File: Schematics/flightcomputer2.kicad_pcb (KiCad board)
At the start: 4 copper layers, 80 x 80 mm, 105 parts, among them J1 Microsemi_FlashPro-JTAG-10, J10 Pyro, J2 Pyro, J4 Drouge, J5 Conn_01x05_Pin, J6 Conn_01x05_Pin, J7 Conn_Coaxial_Small, J8 Micro_SD_Card, J9 USB_C_Receptacle_USB2.0_16P, Q1 IRLML2502TRPBF, Q2 IRLML2502TRPBF, Q3 BC817, Q4 IRLML2502TRPBF, Q6 Q_PMOS_GSD, SW1 SAMZO G4R0015010, SW2 SAMZO G4R0015010, U1 STM32F405RGT6, U2 SN65HVD230, U3 PowerIn, U4 LDL1117-3.3, U5 RFM95W-915S2, U6 Bosch BMP388, U7 LSM6DS3TR-C, U8 W25Q128JVP, U9 H3LIS331DL, Y1 8mhz

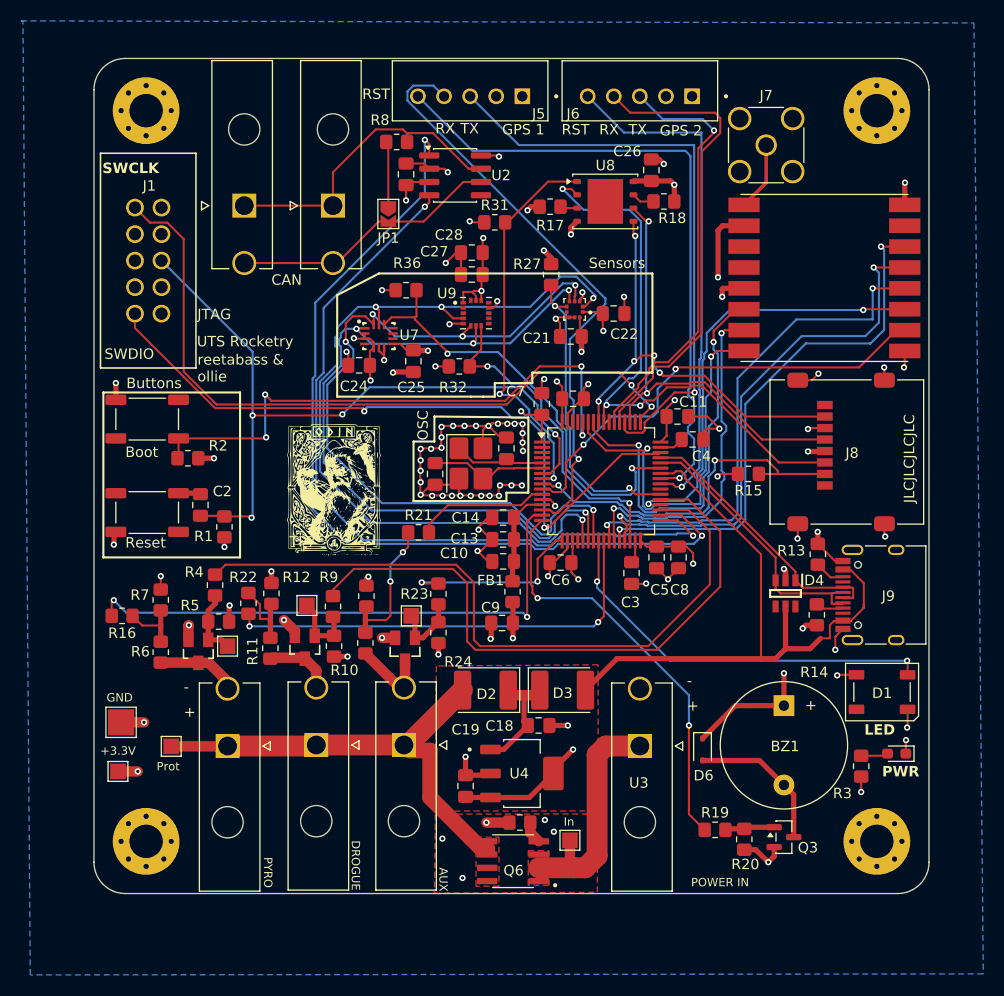
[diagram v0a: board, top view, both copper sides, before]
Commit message: updated .gitignore and fixed rf impedance things
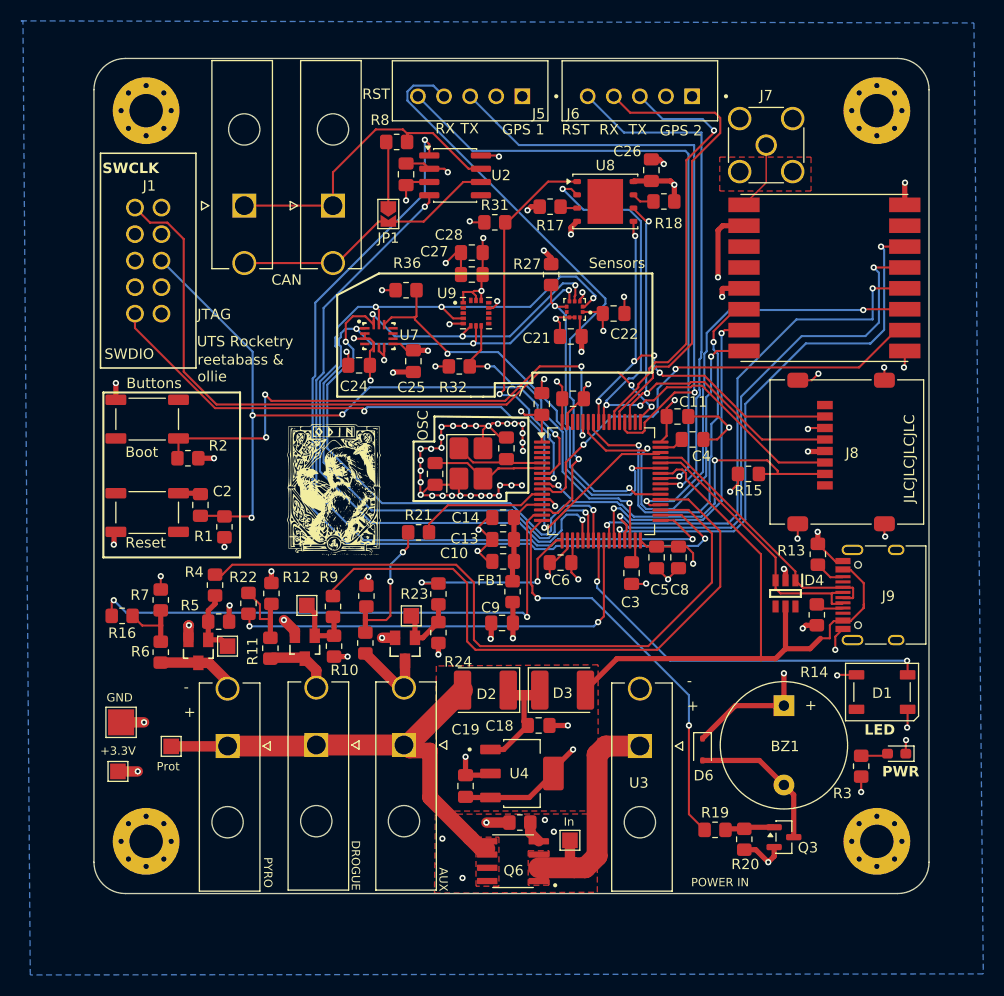
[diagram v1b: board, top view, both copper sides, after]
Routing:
- net GND: track 154.7 -> 156.1 mm
- net /GPS/RESET1: track 62.5 -> 61.3 mm
- net /LoRa/sxDIO2: track 36.9 -> 35.8 mm
- net /Can_transceiver/CAN_TX_2: track 85.7 -> 86.3 mm
